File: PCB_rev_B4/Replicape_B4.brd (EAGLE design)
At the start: 116.8 x 76.4 mm, 258 parts, among them IC1 TMC2100-LA, IC10 74AHC1G126DCK, IC11 74AHC1G126DCK, IC12 TMC2100-LA, IC13 74AHC1G126DCK, IC14 74AHC1G126DCK, IC15 TMC2100-LA, IC16 74AHC1G126DCK, IC17 74AHC1G126DCK, IC18 74AHC1G126DCK, IC19 74AHC1G126DCK, IC2 TMC2100-LA, IC20 74AHC1G126DCK, IC21 74AHC1G126DCK, IC22 74AHC1G126DCK, IC3 74AHC1G126DCK, IC4 74AHC1G126DCK, IC5 TMC2100-LA, IC6 74AHC1G126DCK, IC7 74AHC1G126DCK, IC8 74AHC1G126DCK, IC9 74AHC1G126DCK, P8 F-2X23-, P9 F-2X23-, Q1 AON6758, Q2 AON6758, Q3 AON6758, U1 SN74AHC595PW, U10 RT8268, U11 PCA9685PW, U18 CAT24C256, U19 CD4050BD, U2 SN74AHC595PW, U3 SN74AHC595PW, U4 SN74AHC595PW, U5 SN74AHC595PW, U6 RT8268, U8 FI-RE41S-HFRIGHT_ANGLE, X1 22-05-7038-03, X10 22-05-7038-03, X11 22-05-7028-02, X12 22-05-7048-04, X13 22-05-7038-03, X15 22-05-7048-04, X16 22-05-7048-04, X18 22-05-7048-04, X19 22-05-7038-03, X2 MSTBA4, X20 MSTBA4, X21 MSTBA2, X22 22-05-7038-03, X23 22-05-7038-03, X3 MSTBA2, X4 22-05-7048-04, X5 22-05-7028-02, X6 22-05-7028-02, X7 22-05-7028-02, X8 22-05-7028-02, X9 22-05-7048-04

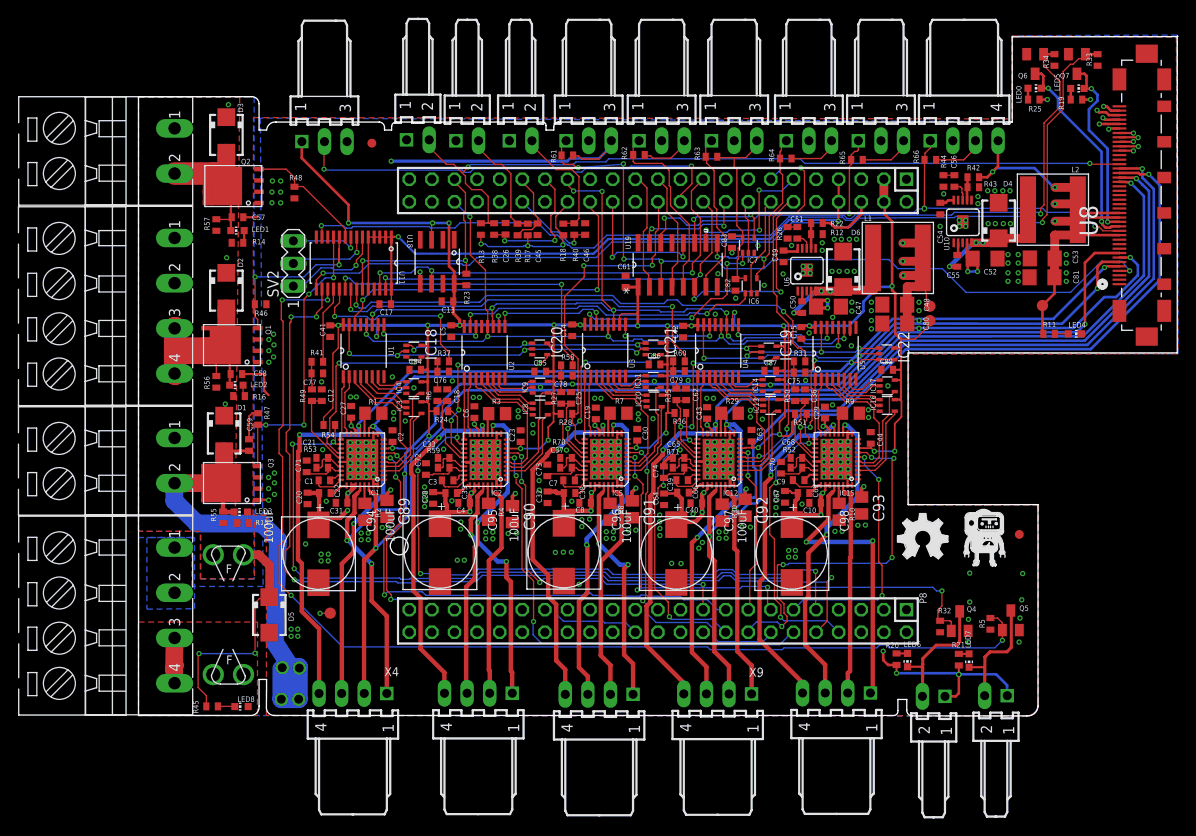
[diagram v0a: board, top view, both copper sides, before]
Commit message: changed the b4 version from 4 layer to 2 layer pcb and removed drc failures
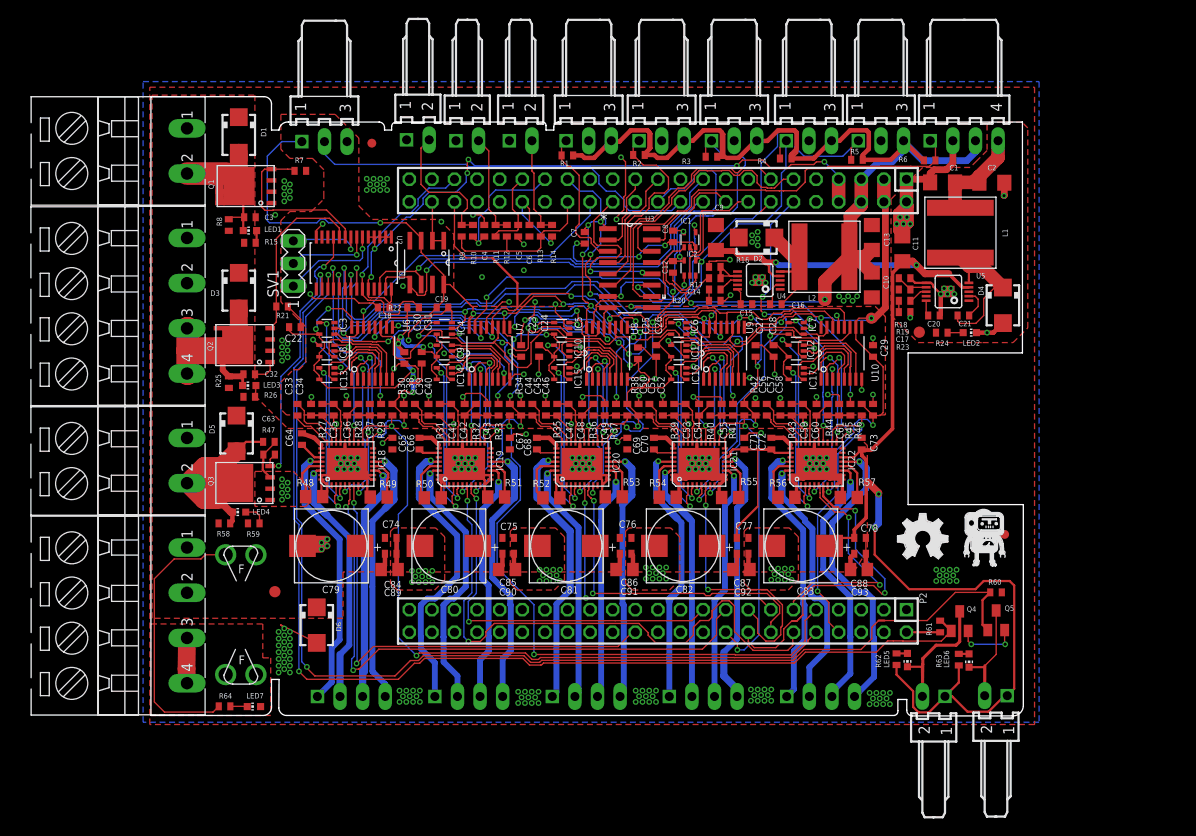
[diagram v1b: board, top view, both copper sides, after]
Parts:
- removed C94, C95, C96, C97, C98: 100uF, Panasonic-EEEFK_EEEFP:RHS1V10MCN1GS
- removed LED0, LED8: blue, led:CHIP-LED0603
- removed Q6, Q7: (no value), semicon-smd-ipc:SOT23
- removed R65, R66: 4.7K, rcl:R0402
- removed R70, R71: 2.2R, rcl:R0402
- removed U$4: CC-BY-SA, Replicape_B3:CC-BY-SA
- removed U11: PCA9685PW, custom:SOP65P640X110-28N
- removed U18: CAT24C256, custom:SOIC127P600X175-8N
- removed U19: CD4050BD, TI-CD4050BD:SOIC127P600X175-16N
- removed X18: 22-05-7048-04, con-molex:7395-04
- removed X19, X22, X23: 22-05-7038-03, con-molex:7395-03
- removed X20: MSTBA4, con-phoenix-508:MSTBA4
- removed X21: MSTBA2, con-phoenix-508:MSTBA2
- added C11: 10uF, rcl:C1206
- added C16: 10nF, rcl:C0402
- added C24, C34: 0.1uF, rcl:C0402
- added C60: 4.7uF, rcl:C0402
- added J500, J501, J502, J503, J504: 22-05-7048-04, con-molex:7395-04
- added U$2: (no value), custom:LOGO_BIG
- added U7, U9: SN74AHC595PW, sn74hc595:SOP65P640X120-16N
- added X14: MSTBA4, con-phoenix-508:MSTBA4
- C1, C9: value 22nF -> 10uF; device rcl:C0402 -> rcl:C1206
- C10, C13, C2: value 0.1uF -> 10uF; device rcl:C0402 -> rcl:C1206
- C12, C18, C25, C26, C46, C62, C65, C68, C75, C76, C77, C78: value 4.7uF -> 0.1uF
- C14, C17: value 0.1uF -> 1nF
- C15, C20: value 0.1uF -> 10nF
- C21: value 4.7uF -> 10nF
- C3: value 22nF -> 4.7nF
- C32, C63: value 0.1uF -> 4.7nF
- C33, C45: value 4.7uF -> 22nF
- C35, C4, C41, C42, C43, C5, C6, C61: value 0.1uF -> 4.7uF
- C47, C48, C53: value 10uF -> 4.7uF; device rcl:C1206 -> rcl:C0402
- C49, C54, C55: value 10nF -> 4.7uF
- C50: value 10nF -> 0.1uF
- C51: value 1nF -> 22nF
- C52: value 10uF -> 0.1uF; device rcl:C1206 -> rcl:C0402
- C56: value 1nF -> 0.1uF
- C57: value 4.7nF -> 22nF
- C58: value 4.7nF -> 0.1uF
- C59: value 4.7nF -> 4.7uF
- C7: value 22nF -> 0.1uF
- C79: value 4.7uF -> 100uF; device rcl:C0402 -> Panasonic-EEEFK_EEEFP:RHS1V10MCN1GS
- C80, C81: value 10uF -> 100uF; device rcl:C1206 -> Panasonic-EEEFK_EEEFP:RHS1V10MCN1GS
- C82, C83: value 0.1uF -> 100uF; device rcl:C0402 -> Panasonic-EEEFK_EEEFP:RHS1V10MCN1GS
- IC1, IC12, IC15, IC2, IC5: value TMC2100-LA -> 74AHC1G126DCK; device we-chip:QFN36-PAD -> 74xx-little-de:SC70-5
- IC18, IC19, IC20, IC21, IC22: value 74AHC1G126DCK -> TMC2100-LA; device 74xx-little-de:SC70-5 -> we-chip:QFN36-PAD
- R1, R2, R3, R30, R4, R7, R8: value 0.1R -> 4.7K; device rcl:R0805 -> rcl:R0402
- R10, R29: value 0.1R -> 10K; device rcl:R0805 -> rcl:R0402
- R11, R14, R28, R32, R33, R36, R45: value 4.7K -> 10K
- R12: value 44.3K,1% -> 4K7, 1%
- R16: value 4.7K -> 10K,1%
- R17: value 4K7, 1% -> 44.3K,1%
- R18: value 4K7, 1% -> 10K,1%
- R19: value 4.7K -> 120K,1%
- R20, R23: value 4.7K -> 39K
- R22: value 10K,1% -> 4.7K
- R26: value 39K -> 4.7K
- R27, R31, R35, R39: value 10K -> 2.2R
- R38, R58, R6, R60: value 10K -> 4.7K
- R42: value 120K,1% -> 4.7K
- R43: value 10K,1% -> 2.2R
- R44: value 39K -> 10K
- R48, R51, R54, R55, R56, R57: value 4.7K -> 0.1R; device rcl:R0402 -> rcl:R0805
- R49, R50: value 10K -> 0.1R; device rcl:R0402 -> rcl:R0805
- R52, R53: value 2.2R -> 0.1R; device rcl:R0402 -> rcl:R0805
- R59: value 2.2R -> 4.7K
- R9: value 0.1R -> 4K7, 1%; device rcl:R0805 -> rcl:R0402
- U$1: value (none) -> CC-BY-SA; device custom:LOGO_BIG -> Replicape_B3:CC-BY-SA
- U1: value SN74AHC595PW -> PCA9685PW; device sn74hc595:SOP65P640X120-16N -> custom:SOP65P640X110-28N
- U10, U6: value RT8268 -> SN74AHC595PW; device SparkFun:MSOP10 -> sn74hc595:SOP65P640X120-16N
- U2: value SN74AHC595PW -> CAT24C256; device sn74hc595:SOP65P640X120-16N -> custom:SOIC127P600X175-8N
- U3: value SN74AHC595PW -> CD4050BD; device sn74hc595:SOP65P640X120-16N -> TI-CD4050BD:SOIC127P600X175-16N
- U4, U5: value SN74AHC595PW -> RT8268; device sn74hc595:SOP65P640X120-16N -> SparkFun:MSOP10
- U8: value FI-RE41S-HFRIGHT_ANGLE -> SN74AHC595PW; device JAE_By_element14_Batch_1:JAE_FI-RE41S-HF -> sn74hc595:SOP65P640X120-16N
- X10: value 22-05-7038-03 -> 22-05-7048-04; device con-molex:7395-03 -> con-molex:7395-04
- X11: value 22-05-7028-02 -> MSTBA2; device con-molex:7395-02 -> con-phoenix-508:MSTBA2
- X12: value 22-05-7048-04 -> MSTBA4; device con-molex:7395-04 -> con-phoenix-508:MSTBA4
- X13: value 22-05-7038-03 -> MSTBA2; device con-molex:7395-03 -> con-phoenix-508:MSTBA2
- X15, X16, X4: value 22-05-7048-04 -> 22-05-7028-02; device con-molex:7395-04 -> con-molex:7395-02
- X2: value MSTBA4 -> 22-05-7028-02; device con-phoenix-508:MSTBA4 -> con-molex:7395-02
- X3: value MSTBA2 -> 22-05-7028-02; device con-phoenix-508:MSTBA2 -> con-molex:7395-02
- X5, X6, X7, X8: value 22-05-7028-02 -> 22-05-7038-03; device con-molex:7395-02 -> con-molex:7395-03
- X9: value 22-05-7048-04 -> 22-05-7038-03; device con-molex:7395-04 -> con-molex:7395-03
- XC1: value MSTBA4-CONNECTOR -> MSTBV2-CONNECTOR; device con-phoenix-508:MSTBA4-CONNECTOR -> con-phoenix-508:MSTBA2-CONNECTOR
- XC4: value MSTBV2-CONNECTOR -> MSTBA4-CONNECTOR; device con-phoenix-508:MSTBA2-CONNECTOR -> con-phoenix-508:MSTBA4-CONNECTOR
- moved LED4 96.1 mm to (11.3, 22.9), turned to 90 degrees
- moved R25 95.9 mm to (10.2, 37.5), turned to 270 degrees
- moved X12 94.3 mm to (0.37, 46.0), turned to 270 degrees
- moved R64 88.1 mm to (9.67, 1.02)
- moved R21 85.8 mm to (16.1, 46.0), turned to 180 degrees
- moved LED2 82.6 mm to (93.4, 43.0), turned to 270 degrees
- moved U$1 80.7 mm to (23.8, 58.6)
- moved LED7 80.5 mm to (13.0, 1.00), turned to 90 degrees
- moved R45 79.1 mm to (80.0, 34.4), turned to 90 degrees
- moved R33 78.0 mm to (40.5, 34.4)
- moved R57 77.4 mm to (79.8, 24.5), turned to 0 degrees
- moved C1 77.1 mm to (90.4, 59.9), turned to 180 degrees
- moved X13 75.7 mm to (0.37, 28.6), turned to 270 degrees
- moved C21 73.8 mm to (92.7, 45.0), turned to 180 degrees
- moved X5 73.5 mm to (50.6, 64.6), turned to 180 degrees
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- renumbered P8 to P2, P9 to P1, SV2 to SV1
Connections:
- removed net AUX_0: U8.10, U8.11
- removed net A_A1: U8.22
- removed net A_A2: U8.21
- removed net A_B1: U8.20
- removed net A_B2: U8.19
- removed net FAN0: Q6.1, R34.2, U11.13
- removed net FAN0_OUT: LED0.C, Q6.3, U8.14
- removed net FAN1: Q7.1, R33.2, U11.15
- removed net FAN1_OUT: LED5.C, Q7.3, U8.15
- removed net IREF_E: C79.1, R35.2, R60.1
- removed net IREF_H: C75.1, R31.1, R50.2
- removed net IREF_X: C77.1, R41.1, R49.2
- removed net IREF_Y: C76.1, R37.1, R6.2
- removed net IREF_Z: C78.1, R27.2, R58.1
- removed net N$21: LED0.A, R25.1
- removed net N$33: C22.1, IC1.29
- removed net N$34: IC3.2, U1.4
- removed net N$47: C33.2, IC2.25, R59.1
- removed net N$48: C35.1, IC2.29
- removed net N$55: IC5.5, U3.3
- removed net N$56: IC2.18, U2.2
- removed net N$70: C39.2, IC12.27
- removed net N$71: IC12.14, R29.2
- removed net N$9: LED5.A, R19.1
- removed net X_CFG1: IC1.4, IC4.4
- removed net X_CFG2: IC1.3, IC3.4
- new net IREF_Z10: C61.1, R44.2, R45.1
- new net IREF_Z6: C49.1, R36.2, R37.1
- new net IREF_Z7: C55.1, R40.2, R41.1
- new net IREF_Z8: C37.1, R28.2, R29.1
- new net IREF_Z9: C43.1, R32.2, R33.1
- new net N$122: IC20.15, J502.4
- new net N$123: IC20.34, J502.2
- new net N$138: IC20.32, J502.1
- new net N$139: IC20.13, J502.3
- new net N$167: IC12.2, U10.6
- new net N$168: IC17.2, U10.4
- new net N$180: IC17.1, U10.5
- new net N$181: C58.1, IC22.26, R43.2
- new net N$224: IC22.32, J500.1
- new net N$225: IC22.13, J500.3
- net +3V3: now also C19.1, C22.1, C24.1, C25.1, C26.1, C27.1, C28.1, C29.1, C31.1, C38.1, C50.1, C56.1, C62.1, C7.1, IC12.5, IC15.5, IC18.8, IC19.8, IC20.8, IC21.8, IC22.8, IC5.5, IC6.5, IC7.5, R22.2, R30.2, R34.2, R38.2, R42.2, R46.2, U10.10, U10.16, U2.3, U2.8, U3.1, U6.10, U6.16, U7.10, U7.16, U8.10, U8.16, U9.10, U9.16, X1.1; no longer C13.1, C14.1, C15.1, C2.1, C41.1, C42.1, C5.1, C61.1, C63.1, C84.1, C85.1, C86.1, C87.1, C88.1, IC1.8, IC12.8, IC15.8, IC18.5, IC19.5, IC2.8, IC20.5, IC21.5, IC22.5, IC5.8, R23.2, R24.2, R28.2, R36.2, R51.2, R54.2, U1.10, U1.16, U18.3, U18.8, U19.1, U2.10, U2.16, U3.10, U3.16, U4.10, U4.16, U5.10, U5.16, X23.1
- net DALLAS_W1: now also X1.2; no longer X23.2
- net DIR_E: now also IC21.7; no longer IC12.7
- net DIR_H: now also IC22.7; no longer IC15.7
- net DIR_X: now also IC18.7; no longer IC1.7
- net DIR_Y: now also IC19.7; no longer IC2.7
- net DIR_Z: now also IC20.7; no longer IC5.7
- net ENABLE: now also R22.1, U1.23; no longer R23.1, U11.23
- net ENABLE_E: now also IC21.22, IC6.4; no longer IC12.22, IC19.4
- net ENABLE_H: now also IC22.22, IC7.4; no longer IC15.22, IC22.4
- net ENABLE_X: now also IC18.22, IC3.4; no longer IC1.22, IC18.4
- net ENABLE_Y: now also IC19.22, IC4.4; no longer IC2.22, IC20.4
- net ENABLE_Z: now also IC20.22, IC5.4; no longer IC21.4, IC5.22
- net END_STOP_X_1: now also U3.2; no longer U19.2
- net END_STOP_X_1_IN: now also R1.1, U3.3, X5.1; no longer R61.1, U19.3, U8.4, X22.1
- net END_STOP_X_2: now also U3.10; no longer U19.10
- net END_STOP_X_2_IN: now also IC2.4, R4.1, U3.9, X8.1; no longer IC6.4, R64.1, U19.9, X10.1
- net END_STOP_Y_1: now also U3.4; no longer U19.4
- net END_STOP_Y_1_IN: now also R2.1, U3.5, X6.1; no longer R62.1, U19.5, X1.1
- net END_STOP_Y_2: now also U3.12; no longer U19.12
- net END_STOP_Y_2_IN: now also IC1.4, R5.1, U3.11, X9.1; no longer IC7.4, R65.1, U19.11, X19.1
- net END_STOP_Z_1: now also U3.6; no longer U19.6
- net END_STOP_Z_1_IN: now also R3.1, U3.7, X7.1; no longer R63.1, U19.7, X13.1
- net END_STOP_Z_2: now also U3.15; no longer U19.15
- net END_STOP_Z_2_IN: now also R6.1, U3.14, X10.1; no longer R66.1, U19.14, U8.13, X12.1
- net EN_EH: now also IC6.2, IC7.2, U9.15; no longer IC19.2, IC22.2, U4.15
- net EN_XYZ: now also IC3.2, IC4.2, IC5.2, U6.15; no longer IC18.2, IC20.2, IC21.2, U1.15
- net E_A1: now also IC21.34, J501.2; no longer IC12.34, U8.27, X9.1
- net E_A2: now also IC21.32, J501.1; no longer IC12.32, U8.26, X9.2
- net E_B1: now also IC21.13, J501.3; no longer IC12.13, U8.25, X9.3
- net E_B2: now also IC21.15, J501.4; no longer IC12.15, U8.24, X9.4
- net FAN2: now also R61.2, U1.16; no longer R32.2, U11.16
- net FAN3: now also R60.2, U1.17; no longer R5.2, U11.17
- net FAULT_E: now also IC21.20, R42.1; no longer IC12.20, R36.1
- net FAULT_H: now also IC22.20, R46.1; no longer IC15.20, R51.1
- net FAULT_X: now also IC18.20, R30.1; no longer IC1.20, R54.1
- net FAULT_Y: now also IC19.20, R34.1; no longer IC2.20, R24.1
- net FAULT_Z: now also IC20.20, R38.1; no longer IC5.20, R28.1
- net GND: now also C1.2, C11.2, C20.2, C22.2, C24.2, C28.2, C3.2, C32.2, C34.2, C35.1, C37.2, C38.2, C41.1, C47.1, C50.2, C53.1, C55.2, C56.2, C59.1, C60.2, C69.1, C7.2, C71.1, C73.1, C79.-, C80.-, C81.-, C82.-, C83.-, C9.2, D2.A, IC1.3, IC12.3, IC15.3, IC18.1, IC18.10, IC18.11, IC18.12, IC18.24, IC18.35, IC18.36, IC18.TP, IC19.1, IC19.10, IC19.11, IC19.12, IC19.24, IC19.35, IC19.36, IC19.TP, IC2.3, IC20.1, IC20.10, IC20.11, IC20.12, IC20.24, IC20.35, IC20.36, IC20.TP, IC21.1, IC21.10, IC21.11, IC21.12, IC21.24, IC21.35, IC21.36, IC21.TP, IC22.1, IC22.10, IC22.11, IC22.12, IC22.24, IC22.35, IC22.36, IC22.TP, IC5.3, LED2.C, R16.2, R18.2, R20.2, R21.1, R23.2, R49.1, R50.1, R51.1, R52.1, R53.1, R54.1, R55.1, R56.1, R57.1, R60.1, R61.1, U1.14, U10.13, U10.8, U2.1, U2.2, U2.4, U4.6, U4.EP, U5.6, U5.EP, U6.13, U6.8, U7.13, U7.8, U8.13, U8.8, U9.13, U9.8, X1.3, X14.1, X14.2, X3.1, X4.1, X5.2, X6.2, X7.2, X8.2, X9.2; no longer C14.2, C17.2, C20.1, C21.1, C28.1, C32.1, C33.1, C37.1, C41.2, C45.2, C47.2, C53.2, C57.2, C59.2, C64.1, C68.1, C70.2, C71.2, C72.2, C73.2, C79.2, C80.2, C81.2, C82.2, C83.2, C94.-, C95.-, C96.-, C97.-, C98.-, D5.A, IC1.1, IC1.10, IC1.11, IC1.12, IC1.24, IC1.35, IC1.36, IC1.TP, IC12.1, IC12.10, IC12.11, IC12.12, IC12.24, IC12.35, IC12.36, IC12.TP, IC15.1, IC15.10, IC15.11, IC15.12, IC15.24, IC15.35, IC15.36, IC15.TP, IC18.3, IC19.3, IC2.1, IC2.10, IC2.11, IC2.12, IC2.24, IC2.35, IC2.36, IC2.TP, IC20.3, IC21.3, IC22.3, IC5.1, IC5.10, IC5.11, IC5.12, IC5.24, IC5.35, IC5.36, IC5.TP, LED4.C, Q6.2, Q7.2, R1.1, R10.1, R2.1, R22.2, R26.2, R29.1, R3.1, R30.1, R32.1, R33.1, R34.1, R4.1, R43.2, R44.2, R46.1, R5.1, R8.1, R9.1, U1.13, U1.8, U10.6, U10.EP, U11.14, U18.1, U18.2, U18.4, U19.8, U2.13, U2.8, U3.13, U4.13, U4.8, U5.13, U5.8, U6.6, U6.EP, U8.18, U8.23, U8.3, U8.30, U8.41, U8.9, X1.2, X11.1, X12.2, X13.2, X19.2, X2.2, X22.2, X23.3, X7.1, X8.1
- net HEATER_E: now also U1.11; no longer U11.11
- net HEATER_E_OUT: now also C63.1, D5.A, LED4.C, R58.1, X13.2; no longer C59.1, D1.A, LED3.C, R55.1, U8.31, U8.32, U8.33, U8.34, U8.35, X3.2
- net HEATER_H: now also Q1.4, R7.2, U1.9; no longer Q2.4, R48.2, U11.9
- net HEATER_HBP: now also Q2.4, R21.2, U1.10; no longer Q1.4, R46.2, U11.10
- net I2C2_SCL: now also U1.26, U2.6; no longer U11.26, U18.6
- net I2C2_SDA: now also U1.27, U2.5; no longer U11.27, U18.5
- net IREF_E_RAW: now also R41.2, U1.21; no longer R60.2, U11.21
- net IREF_H_RAW: now also R45.2, U1.22; no longer R31.2, U11.22
- net IREF_X_RAW: now also R29.2, U1.18; no longer R41.2, U11.18
- net IREF_Y_RAW: now also R33.2, U1.19; no longer R37.2, U11.19
- net IREF_Z_RAW: now also R37.2, U1.20; no longer R58.2, U11.20
- net N$1: now also U1.6; no longer U11.6
- net N$100: now also IC22.14, R57.2; no longer IC15.5, U5.3
- net N$101: now also IC22.33, R56.2; no longer IC15.18, U5.2
- net N$102: now also C60.1, IC22.23, R44.1; no longer IC15.19, U5.1
- net N$103: now also C57.1, IC22.28; no longer IC17.1, U5.7
- net N$104: now also IC17.4, IC22.3; no longer IC17.2, U5.6
- net N$105: now also IC22.15, J500.4; no longer IC16.1, U5.5
- net N$106: now also IC22.34, J500.2; no longer IC16.2, U5.4
- net N$107: now also C59.2, IC22.25, R43.1; no longer C70.1, IC15.26, R52.2
- net N$108: now also C72.1, IC22.29; no longer C71.1, IC1.26, R53.2
- net N$109: now also IC12.4, IC22.4; no longer C73.1, IC5.26, R70.2
- net N$110: now also IC22.5, U10.3; no longer C72.1, IC2.26, R59.2
- net N$111: now also IC22.18, U10.2; no longer C74.1, IC12.26, R71.2
- net N$113: now also IC22.19, U10.1; no longer IC15.13, X18.3
- net N$114: now also LED6.C, X16.2; no longer LED7.C, X6.2
- net N$115: now also LED5.C, X15.2; no longer LED6.C, X5.2
- net N$117: now also LED5.A, R62.1; no longer LED6.A, R20.1
- net N$118: now also LED6.A, R63.1; no longer LED7.A, R21.1
- net N$119: now also IC12.1, U10.7; no longer IC15.32, X18.1
- net N$12: now also IC15.4, IC20.3; no longer C9.2, IC15.27
- net N$120: now also U1.8; no longer U11.8
- net N$121: now also U1.7; no longer U11.7
- net N$127: now also LED4.A, R59.1; no longer LED3.A, R15.1
- net N$129: now also R15.1; no longer R14.1
- net N$13: now also C47.2, IC20.25, R35.1; no longer IC15.14, R9.2
- net N$130: now also LED3.A, R26.1; no longer LED2.A, R16.1
- net N$14: now also C68.1, IC20.29; no longer C7.2, IC5.27
- net N$15: now also IC10.4, IC20.4; no longer IC5.14, R7.2
- net N$16: now also IC20.5, U8.3; no longer C1.1, IC1.28
- net N$17: now also IC20.18, U8.2; no longer C1.2, IC1.27
- net N$18: now also IC20.19, U8.1; no longer IC1.14, R1.2
- net N$19: now also IC10.1, U8.7; no longer IC1.33, R2.2
- net N$2: now also C45.2, IC20.27; no longer IC2.13, X15.3
- net N$20: now also IC10.2, U8.6; no longer C12.1, IC1.23, R49.1
- net N$22: now also IC15.2, U8.4; no longer IC2.32, X15.1
- net N$23: now also R16.1, R17.2, U4.7; no longer R12.2, R22.1, U6.7
- net N$233: now also R18.1, R19.2, U5.7; no longer R42.2, R43.1, U10.7
- net N$238: now also C21.2, L1.P$2, U5.5; no longer C55.2, L2.P$2, U10.5
- net N$24: now also IC15.1, U8.5; no longer IC5.33, R8.2
- net N$240: now also R13.1, R14.1, X4.2; no longer R18.1, R40.1, X11.2
- net N$241: now also R11.1, R12.1, X3.2; no longer R17.1, R39.1, X7.2
- net N$242: now also C32.1, D3.A, LED3.C, Q2.5, Q2.6, Q2.7, Q2.8, Q2.TH, R25.1, X12.3, X12.4; no longer C58.1, D2.A, LED2.C, Q1.5, Q1.6, Q1.7, Q1.8, Q1.TH, R56.1, X20.3, X20.4
- net N$243: now also C20.1, U5.10; no longer C54.1, U10.10
- net N$244: now also C17.1, U5.8; no longer C56.1, U10.8
- net N$245: now also C21.1, U5.2; no longer C55.1, U10.2
- net N$246: now also C17.2, R23.1; no longer C56.2, R44.1
- net N$25: now also C16.2, D2.C, L2.P$2, U4.5; no longer C50.2, D6.C, L1.P$2, U6.5
- net N$26: now also C46.1, IC20.26, R35.2; no longer C25.1, IC5.23, R27.1
- net N$27: now also C51.2, IC21.27; no longer C7.1, IC5.28
- net N$28: now also IC21.14, R55.2; no longer IC10.4, IC5.3
- net N$29: now also IC21.33, R54.2; no longer IC5.15, X16.4
- net N$3: now also IC20.14, R53.2; no longer C3.2, IC2.27
- net N$30: now also C54.1, IC21.23, R40.1; no longer IC15.33, R10.2
- net N$31: now also C51.1, IC21.28; no longer C21.2, IC1.25, R53.1
- net N$32: now also IC16.4, IC21.3; no longer IC5.32, X16.1
- net N$35: now also C53.2, IC21.25, R39.1; no longer IC2.14, R3.2
- net N$36: now also C70.1, IC21.29; no longer IC2.33, R4.2
- net N$37: now also IC11.4, IC21.4; no longer IC5.13, X16.3
- net N$38: now also IC21.5, U9.3; no longer C18.1, IC2.23, R6.1
- net N$4: now also IC20.33, R52.2; no longer IC4.1, U1.7
- net N$40: now also IC21.18, U9.2; no longer IC3.1, U1.5
- net N$41: now also IC21.19, U9.1; no longer C3.1, IC2.28
- net N$42: now also IC11.1, U9.7; no longer IC2.3, IC8.4
- net N$43: now also IC11.2, U9.6; no longer IC1.19, U1.1
- net N$44: now also IC16.2, U9.4; no longer IC1.5, U1.3
- net N$45: now also IC16.1, U9.5; no longer IC2.15, X15.4
- net N$46: now also C52.1, IC21.26, R39.2; no longer IC2.34, X15.2
- net N$49: now also C33.2, IC18.27; no longer IC2.4, IC9.4
- net N$5: now also C48.1, IC20.23, R36.1; no longer IC4.2, U1.6
- net N$50: now also IC18.14, R49.2; no longer IC5.34, X16.2
- net N$51: now also IC18.33, R48.2; no longer C37.2, IC5.25, R70.1
- net N$52: now also C36.1, IC18.23, R28.1; no longer C38.1, IC5.29
- net N$53: now also C33.1, IC18.28; no longer IC2.5, U2.3
- net N$54: now also IC13.4, IC18.3; no longer IC11.4, IC5.4
- net N$57: now also C35.2, IC18.25, R27.1; no longer IC5.18, U3.2
- net N$58: now also C64.1, IC18.29; no longer IC5.19, U3.1
- net N$59: now also IC18.4, IC8.4; no longer IC11.1, U3.7
- net N$6: now also C45.1, IC20.28; no longer IC1.18, U1.2
- net N$60: now also C15.1, U4.10; no longer C49.1, U6.10
- net N$61: now also IC18.5, U6.3; no longer IC11.2, U3.6
- net N$62: now also IC18.18, U6.2; no longer IC10.1, U3.5
- net N$63: now also IC18.19, U6.1; no longer IC10.2, U3.4
- net N$64: now also C3.1, D1.A, Q1.5, Q1.6, Q1.7, Q1.8, Q1.TH, R8.1, X11.2; no longer C57.1, D3.A, Q2.5, Q2.6, Q2.7, Q2.8, Q2.TH, R57.1, X21.2
- net N$65: now also IC8.1, U6.7; no longer IC2.19, U2.1
- net N$66: now also IC8.2, U6.6; no longer IC9.1, U2.7
- net N$67: now also IC13.2, U6.4; no longer IC9.2, U2.6
- net N$68: now also IC13.1, U6.5; no longer IC8.1, U2.5
- net N$69: now also C34.1, IC18.26, R27.2; no longer IC8.2, U2.4
- net N$72: now also C39.2, IC19.27; no longer IC12.33, R30.2
- net N$73: now also C16.1, U4.2; no longer C50.1, U6.2
- net N$74: now also IC19.14, R51.2; no longer C62.1, IC12.23, R35.1
- net N$75: now also IC19.33, R50.2; no longer C39.1, IC12.28
- net N$76: now also C42.1, IC19.23, R32.1; no longer IC12.3, IC13.4
- net N$79: now also C39.1, IC19.28; no longer C65.2, IC12.25, R71.1
- net N$8: now also LED7.C, R64.2; no longer LED8.C, R45.2
- net N$80: now also IC14.4, IC19.3; no longer C66.1, IC12.29
- net N$81: now also IC19.15, J503.4; no longer IC12.4, IC14.4
- net N$82: now also IC19.34, J503.2; no longer IC12.5, U4.3
- net N$83: now also C41.2, IC19.25, R31.1; no longer IC12.18, U4.2
- net N$84: now also C66.1, IC19.29; no longer IC12.19, U4.1
- net N$85: now also IC19.4, IC9.4; no longer IC14.1, U4.7
- net N$86: now also IC19.5, U7.3; no longer IC14.2, U4.6
- net N$87: now also IC19.18, U7.2; no longer IC13.1, U4.5
- net N$88: now also C14.1, U4.8; no longer C51.1, U6.8
- net N$89: now also IC19.19, U7.1; no longer C36.1, IC15.23, R50.1
- net N$90: now also IC9.1, U7.7; no longer C9.1, IC15.28
- net N$91: now also IC9.2, U7.6; no longer IC15.3, IC16.4
- net N$92: now also IC14.2, U7.4; no longer IC15.15, X18.4
- net N$93: now also IC14.1, U7.5; no longer IC13.2, U4.4
- net N$94: now also C40.1, IC19.26, R31.2; no longer IC15.34, X18.2
- net N$95: now also IC19.32, J503.1; no longer C68.2, IC15.25, R52.1
- net N$96: now also LED2.A, R24.1; no longer LED4.A, R11.1
- net N$97: now also C14.2, R20.1; no longer C51.2, R26.1
- net N$98: now also IC19.13, J503.3; no longer C69.1, IC15.29
- net N$99: now also C57.2, IC22.27; no longer IC15.4, IC17.4
- net SERVO_0: now also IC2.2; no longer IC6.2
- net SERVO_0_EN: now also IC2.1, U7.15; no longer IC6.1, U2.15
- net SERVO_1: now also IC1.2; no longer IC7.2
- net SERVO_1_EN: now also IC1.1, U8.15; no longer IC7.1, U3.15
- net SER_2: now also U6.9, U7.14; no longer U1.9, U2.14
- net SER_3: now also U7.9, U8.14; no longer U2.9, U3.14
- net SER_4: now also U8.9, U9.14; no longer U3.9, U4.14
- net SER_5: now also U10.14, U9.9; no longer U4.9, U5.14
- net SPI1_CS1: now also U10.12, U6.12, U7.12, U8.12, U9.12; no longer U1.12, U2.12, U3.12, U4.12, U5.12
- net SPI1_MOSI: now also U6.14; no longer U1.14
- net SPI1_SCLK: now also U10.11, U6.11, U7.11, U8.11, U9.11; no longer U1.11, U2.11, U3.11, U4.11, U5.11
- net STEP_E: now also IC21.6; no longer IC12.6
- net STEP_H: now also IC22.6; no longer IC15.6
- net STEP_X: now also IC18.6; no longer IC1.6
- net STEP_Y: now also IC19.6; no longer IC2.6
- net STEP_Z: now also IC20.6; no longer IC5.6
- net SYS_5V: now also C18.1, U1.1, U1.2, U1.24, U1.28, U1.3, U1.4, U1.5; no longer C17.1, U11.1, U11.2, U11.24, U11.28, U11.3, U11.4, U11.5
- net TERM_EXT1: now also C4.1, R10.2; no longer C26.1, R38.2
- net TERM_EXT2: now also C6.1, R14.2; no longer C46.1, R40.2
- net TERM_HBP: now also C5.1, R11.2; no longer C45.1, R39.2
- net THERM_EXT1_IN: now also R10.1, R9.1, X2.2; no longer R13.1, R38.1, U8.28, X8.2
- net TRISTATE_STEPPERS: now also IC3.1, IC4.1, IC5.1, IC6.1, IC7.1, U10.15; no longer IC18.1, IC19.1, IC20.1, IC21.1, IC22.1, U5.15
- net VDD_12V: now also C1.1, C2.1, L1.P$1, R19.1, R24.2, X10.4; no longer C53.1, C81.1, L2.P$1, R11.2, R42.1, U8.12, U8.16, U8.17, X12.4
- net VDD_5V: now also C10.1, C12.1, C13.1, C8.1, IC1.5, IC2.5, L2.P$1, R1.2, R17.1, R2.2, R3.2, R4.2, R5.2, R6.2, X5.3, X6.3, X7.3, X8.3, X9.3; no longer C48.1, C80.1, C82.1, C83.1, IC6.5, IC7.5, L1.P$1, R12.1, R61.2, R62.2, R63.2, R64.2, R65.2, R66.2, X1.3, X12.3, X13.3, X19.3, X22.3
- net VDD_ADC: now also R12.2, R9.2; no longer R17.2, R18.2
- net VDD_IN: now also C11.1, C65.2, C68.2, C70.2, C71.2, C72.2, C73.2, C74.1, C75.1, C76.1, C77.1, C78.1, C79.+, C80.+, C81.+, C82.+, C83.+, C84.1, C85.1, C86.1, C87.1, C88.1, C9.1, D6.C, IC18.16, IC18.30, IC18.31, IC19.16, IC19.30, IC19.31, IC20.16, IC20.30, IC20.31, IC21.16, IC21.30, IC21.31, IC22.16, IC22.30, IC22.31, R26.2, R58.2, R59.2, R62.2, R63.2, R64.1, R8.2, U4.4, U5.4, X11.1, X12.1, X12.2, X13.1, X15.1, X16.1; no longer C10.1, C19.1, C20.2, C22.2, C27.1, C28.2, C29.1, C31.1, C32.2, C35.2, C38.2, C4.1, C40.1, C43.1, C47.1, C52.1, C6.1, C8.1, C94.+, C95.+, C96.+, C97.+, C98.+, D2.C, IC1.16, IC1.30, IC1.31, IC12.16, IC12.30, IC12.31, IC15.16, IC15.30, IC15.31, IC2.16, IC2.30, IC2.31, IC5.16, IC5.30, IC5.31, R14.2, R16.2, R19.2, R20.2, R21.2, R45.1, R55.2, R56.2, R57.2, U10.4, U6.4, U8.36, U8.37, U8.38, U8.39, U8.40, X20.1, X20.2, X21.1, X3.1, X5.1, X6.1
- net VIN: now also LED7.A, X14.3, X14.4; no longer LED8.A, X2.3, X2.4
- net X_A1: now also IC18.34, J504.2; no longer IC1.34, U8.8, X4.2
- net X_A2: now also IC18.32, J504.1; no longer IC1.32, U8.7, X4.1
- net X_B1: now also IC18.13, J504.3; no longer IC1.13, U8.6, X4.3
- net X_B2: now also IC18.15, J504.4; no longer IC1.15, U8.5, X4.4
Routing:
- net GND: track 34.2 -> 365.9 mm
- net FAN1: track 109.0 -> 0.00 mm, vias 2 -> 0
- net FAN0: track 106.7 -> 0.00 mm, vias 2 -> 0
- net X_A2: track 135.5 -> 30.7 mm, vias 3 -> 1
- net X_A1: track 130.3 -> 28.2 mm, vias 2 -> 1
- net X_B2: track 131.9 -> 29.8 mm, vias 3 -> 1
- net X_B1: track 127.3 -> 27.3 mm, vias 3 -> 1
- net +3V3: track 282.2 -> 366.6 mm, vias 27 -> 41
- net E_B1: track 105.9 -> 27.0 mm, vias 3 -> 1
- net E_B2: track 106.8 -> 30.1 mm, vias 3 -> 1
- net E_A2: track 106.2 -> 30.0 mm, vias 2 -> 1
- net E_A1: track 102.0 -> 27.5 mm, vias 2 -> 1
- net THERM_EXT1_IN: track 89.6 -> 15.6 mm, vias 2 -> 0
- net END_STOP_X_1_IN: track 85.8 -> 16.5 mm, vias 5 -> 0
- net VDD_IN: track 157.6 -> 220.4 mm, vias 41 -> 4
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- added copper zone on layer 1, net VDD_12V
- removed copper zone on layer 2, net GND
- removed copper zone on layer 3, net HEATER_E_OUT
- removed copper zone on layer 3, net VDD_12V
- removed copper zone on layer 3, net VDD_5V
- removed copper zone on layer 3, net VDD_ADC
- removed copper zone on layer 16, net VDD_IN
- removed copper zone on layer 3, net VDD_IN
- removed copper zone on layer 3, net VIN
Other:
- board size 116.8 x 76.4 mm -> 98.1 x 69.6 mm
